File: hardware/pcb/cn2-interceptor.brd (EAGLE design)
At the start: 31.5 x 26 mm, 4 parts, among them J1 JST-XH 4P, J2 JST-XH 4P, U1 XIAO ESP32-C3, U2 4CH BSS138

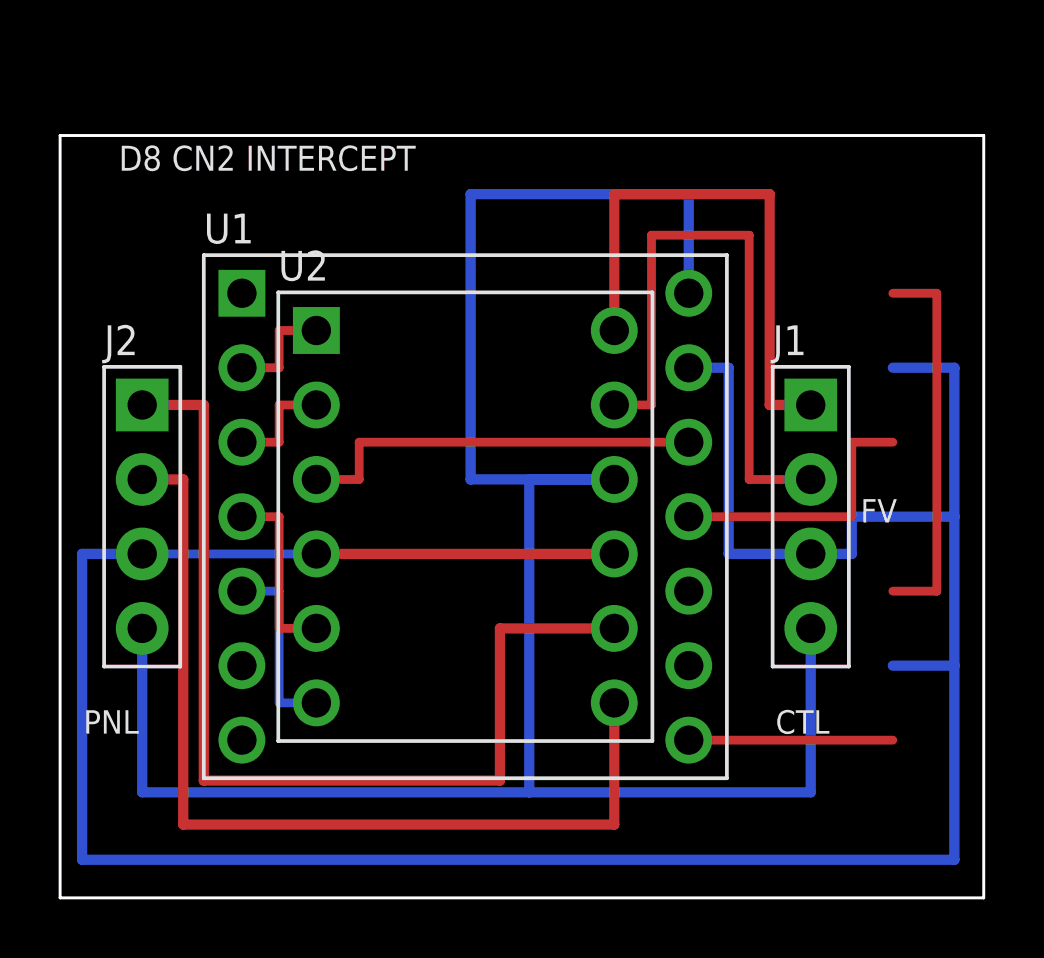
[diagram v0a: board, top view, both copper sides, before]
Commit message: pcb: 18.6 x 27 mm — connectors on opposite edges, flow relay dropped
39% less area and 41% narrower than the 31.5 x 26 board, which is the
dimension that decides whether it fits inside the appliance. Nothing about
the CN2 interception changes.

What made it small: the XIAO's two pad rows are 15.24 mm apart, so anything
standing beside them adds width directly, and the old board had a connector
on each side. Moving both to the top and bottom edges leaves nothing outside
the module except one routing lane -- shared by +5V on top and GND on the
bottom -- so the width is now pad block + lane + two edges, fully accounted
for and with nothing left in it. Each CN2 signal pin sits directly under the
middle corridor and climbs straight out of its own pad into its shifter pin,
turning once, so the four signals need no side lane at all.

The flow-meter relay (J3/J4) is gone, per Kai's call. Its six pins could not
share an edge with the CN2 connectors, so they were what forced the
connectors back onto the sides: that one feature cost more board than
everything else on it. The two hard-won warnings about it (the C3 is not 5 V
tolerant with no channel left to shift FV, and cutting the line strands the
meter's pull-up on the far side) are kept in the README for whoever re-adds
it.

Which connector goes on which edge is load-bearing, not cosmetic. Routing
forces LV1..LV4 onto D1..D4 in order -- they share a 0.94 mm channel and any
other order overlaps four deep -- and D1..D4 are GPIO3,4,5,6. The firmware's
as-built map puts the controller on GPIO5/6, which are the shifter's upper
channels, so the controller enters from the top. Get it backwards and the
board still works but only after swapping four defines, and a pin map that
disagrees with the copper does not announce itself: frames just stop
decoding. gen_pcb.py now reads firmware/include/config.h and fails on a
mismatch rather than leaving that to a comment.

Two new checks, both of which caught something real:

  MECHANICAL  th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
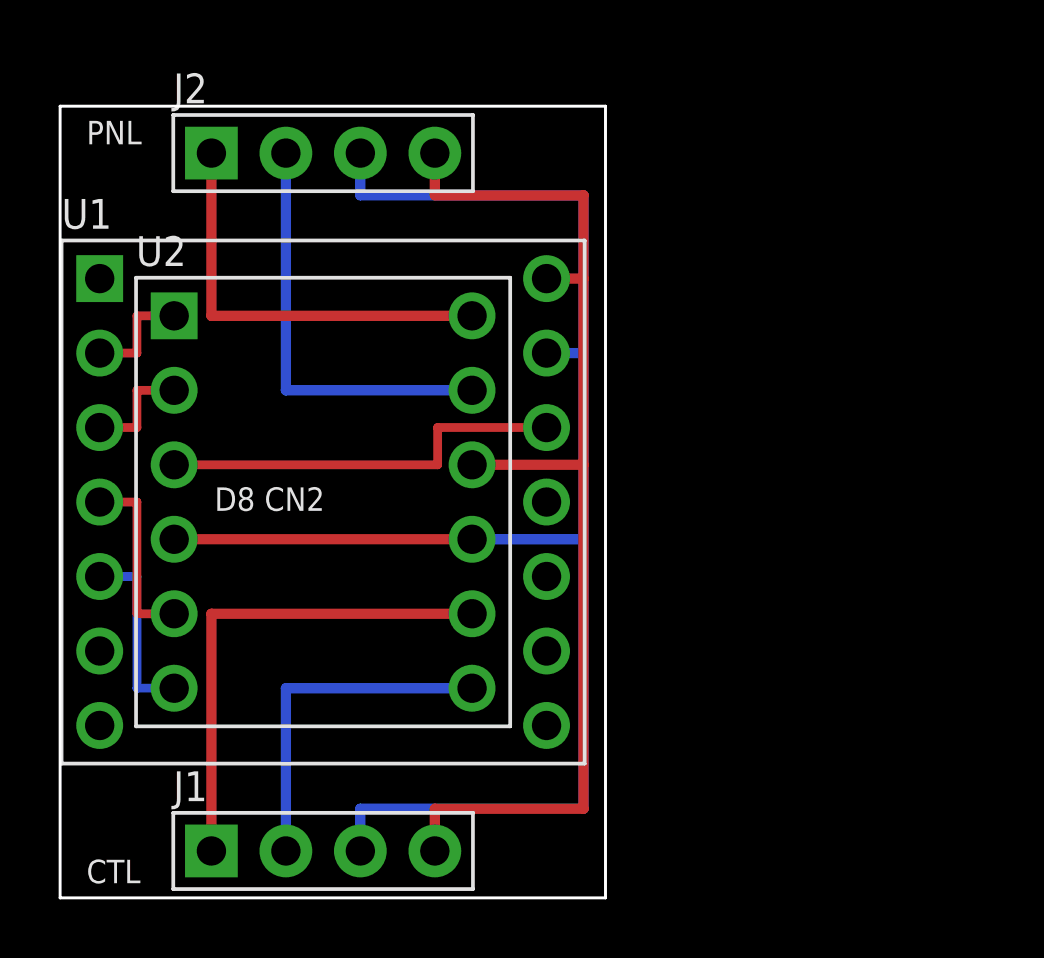
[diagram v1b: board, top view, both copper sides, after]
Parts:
- moved J1 25.5 mm to (5.16, 1.60)
- moved J2 8.91 mm to (5.16, 25.4)
- moved U1 4.88 mm to (1.35, 21.1)
- moved U2 4.88 mm to (3.89, 19.9)
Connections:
- removed net FLOW_IN: J3.SIG, U1.D10
- removed net FLOW_OUT: J4.SIG, U1.D7
- removed net FV_VCC: J3.VCC, J4.VCC
- net CH1_HV: now also J2.1; no longer J1.1
- net CH2_HV: now also J2.2; no longer J1.2
- net CH3_HV: now also J1.1; no longer J2.1
- net CH4_HV: now also J1.2; no longer J2.2
- net GND: no longer J3.GND, J4.GND
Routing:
- net GND: track 96.0 -> 54.2 mm
- net +5V: track 73.0 -> 39.0 mm
- net CH4_HV: track 32.0 -> 11.9 mm
- net CH3_HV: track 34.1 -> 17.0 mm
- net FV_VCC: track 13.2 -> 0.00 mm
- net FLOW_IN: track 9.50 -> 0.00 mm
- net FLOW_OUT: track 6.96 -> 0.00 mm
- net CH2_HV: track 20.8 -> 14.4 mm
- net CH1_HV: track 18.5 -> 14.4 mm
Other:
- board size 31.5 x 26 mm -> 18.6 x 27 mm
- board text added: "D8 CN2"
- board text removed: "D8 CN2 INTERCEPT"
- board text removed: "FV"

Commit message: pcb: silkscreen marks the XIAO's USB end and the JST latch side
Two orientation mistakes this board could not previously warn you about, both
of which look correct after assembly:

  USB + arrow   D0 and 5V are the pins at the XIAO's USB end and both sit at
                the low-y end here, so the port faces the PANEL connector.
                A 2x7 header is physically symmetric, so nothing stops the
                module going in backwards -- every signal then lands on the
                wrong pin.
  [ ] bracket   An XH shroud is not symmetric; the ramp the cable clip engages
                is on one long side. Both connectors are marked with the latch
                facing the nearest board edge, so the clips stay reachable once
                the board is mounted. Backwards, the clip faces the board and
                cannot be released.

The silkscreen engine could only draw glyphs, so this adds a Line primitive
and teaches both exporters about it -- the marks would otherwise have appeared
in my Gerbers and the panel but not in the .brd/.kicad_pcb that actually get
imported.

New silk_check(): silkscreen must stay on the board and off every pad. It
caught its own first draft -- the bracket ticks turned outward and ran 0.23 mm
past the edge, where the fab would simply have dropped them. Also bumped the
USB text to 0.8 mm, KiCad's minimum silk height.

Documented while marking it: the USB port faces J2 about 1.4 mm away. On
sockets it clears the JST housing, but a MATED panel cable stands about as
tall as the USB plug and sits right in front. Plug USB in first, or move both
connectors to the top edge (~21 x 24 mm, same area, USB clear). Worth naming
because a session on this project ran entirely over USB serial with the radio
off, so losing USB access after assembly is a real cost.

DRC PASS, connectivity PASS, mechanical PASS, KiCad DRC back to the 4 known
lib_footprint_issues, panel regenerated.

Co-Authored-By: Claude Opus 5 <noreply@anthropic.com>
Cl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
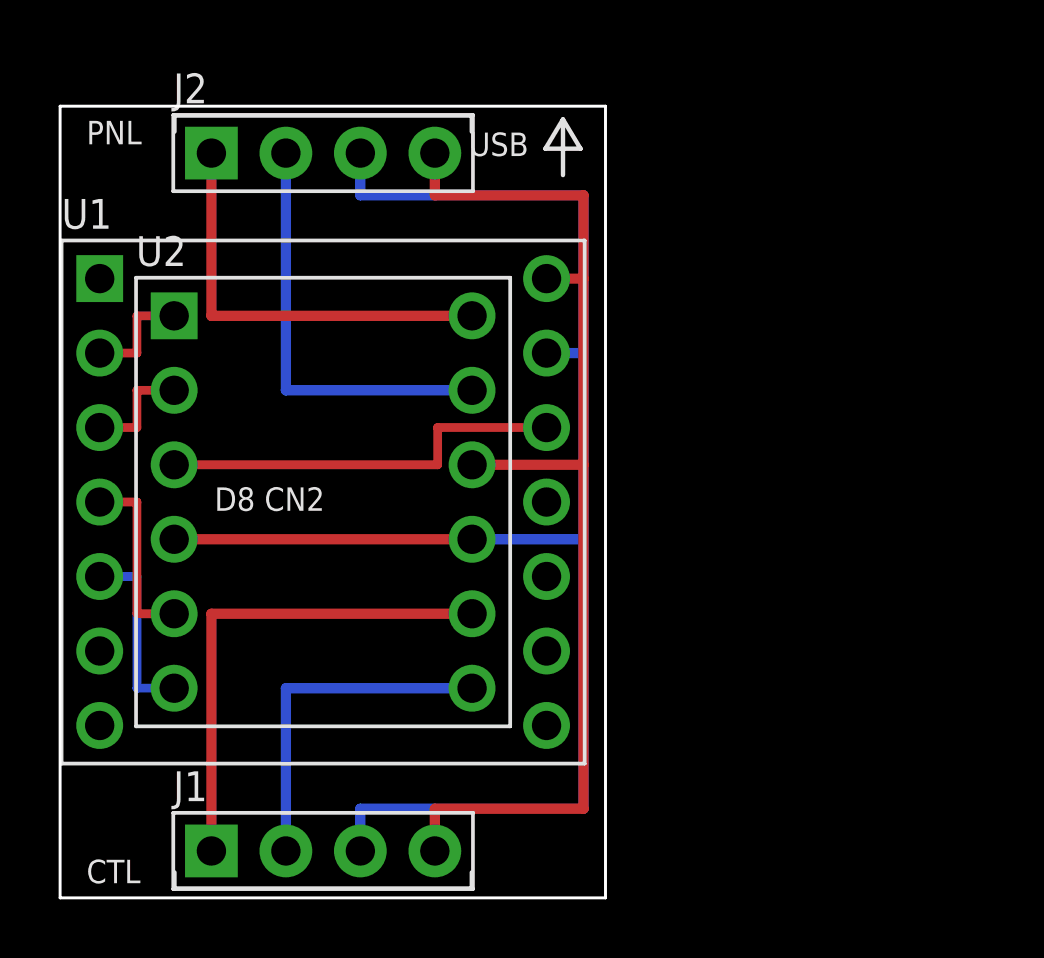
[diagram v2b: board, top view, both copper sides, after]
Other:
- board text added: "USB"
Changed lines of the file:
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@@
 <text x="0.900" y="0.500" size="0.800" layer="21">CTL</text>
 <text x="5.265" y="13.200" size="0.800" layer="21">D8 CN2</text>
+<text x="13.950" y="25.300" size="0.800" layer="21">USB</text>
+<wire x1="3.900" y1="26.680" x2="14.040" y2="26.680" width="0.15" layer="21"/>
+<wire x1="3.900" y1="26.680" x2="3.900" y2="26.130" width="0.15" layer="21"/>
+<wire x1="14.040" y1="26.680" x2="14.040" y2="26.130" width="0.15" layer="21"/>
+<wire x1="3.900" y1="0.320" x2="14.040" y2="0.320" width="0.15" layer="21"/>
+<wire x1="3.900" y1="0.320" x2="3.900" y2="0.870" width="0.15" layer="21"/>
+<wire x1="14.040" y1="0.320" x2="14.040" y2="0.870" width="0.15" layer="21"/>
+<wire x1="17.150" y1="26.550" x2="16.550" y2="25.550" width="0.15" layer="21"/>
+<wire x1="17.150" y1="26.550" x2="17.750" y2="25.550" width="0.15" layer="21"/>
+<wire x1="16.550" y1="25.550" x2="17.750" y2="25.550" width="0.15" layer="21"/>
+<wire x1="17.150" y1="26.550" x2="17.150" y2="24.650" width="0.15" layer="21"/>
 </plain>
 <attributes/><variantdefs/>
